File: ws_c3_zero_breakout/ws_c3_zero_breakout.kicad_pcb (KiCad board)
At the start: 2 copper layers, 27 x 30 mm, 10 parts, among them J1 LEFT WING, J2 RIGHT WING, U1 QMI8658C, U2 QMC5883L

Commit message: comment and label change
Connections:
- net /GP20 renamed /UART0_RX
- net /GP21 renamed /UART0_TX
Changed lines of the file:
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@@
 			(layers "*.Cu" "*.Mask")
 			(remove_unused_layers no)
-			(net "/GP20")
+			(net "/UART0_RX")
 			(pinfunction "Pin_8_8")
 			(pintype "passive+no_connect")
@@
 			(layers "*.Cu" "*.Mask")
 			(remove_unused_layers no)
-			(net "/GP21")
+			(net "/UART0_TX")
 			(pinfunction "Pin_9_9")
 			(pintype "passive+no_connect")
@@
 		(effects
 			(font
-				(size 1 1)
+				(size 0.8 0.8)
 				(thickness 0.1)
 			)

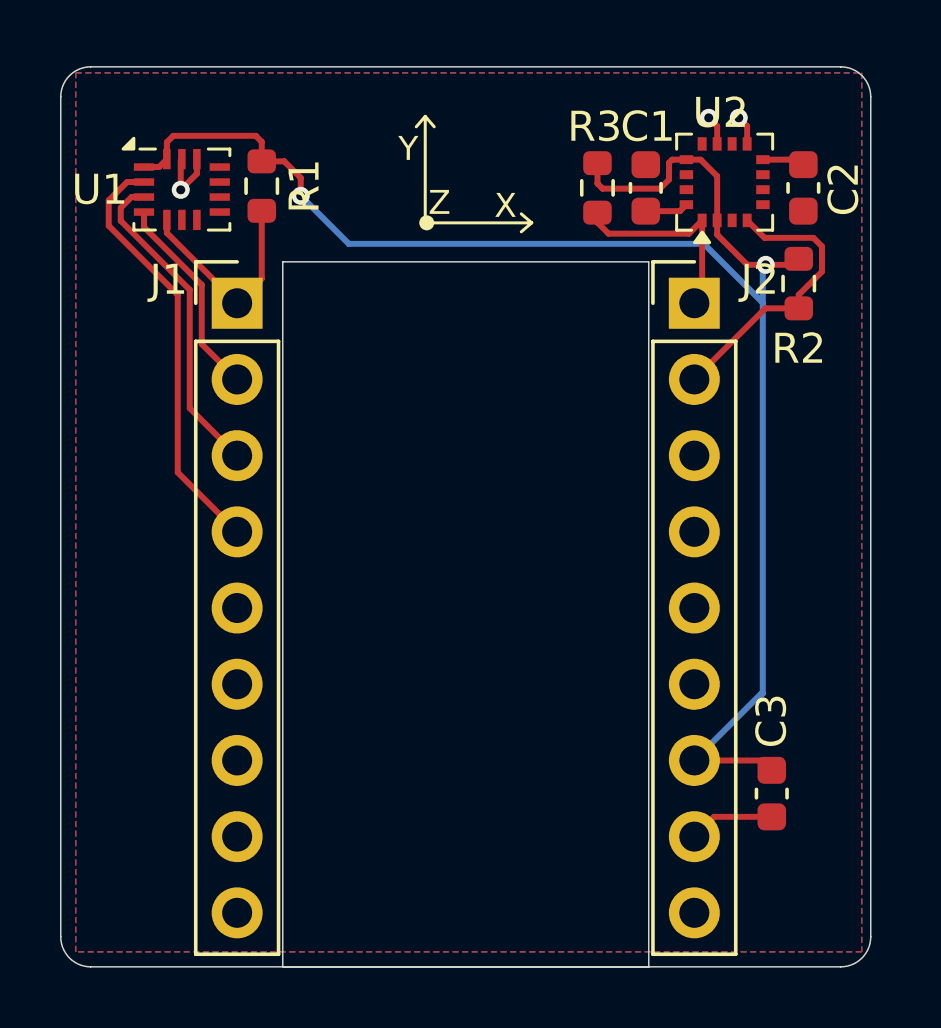
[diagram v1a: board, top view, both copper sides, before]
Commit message: board edgecut fix
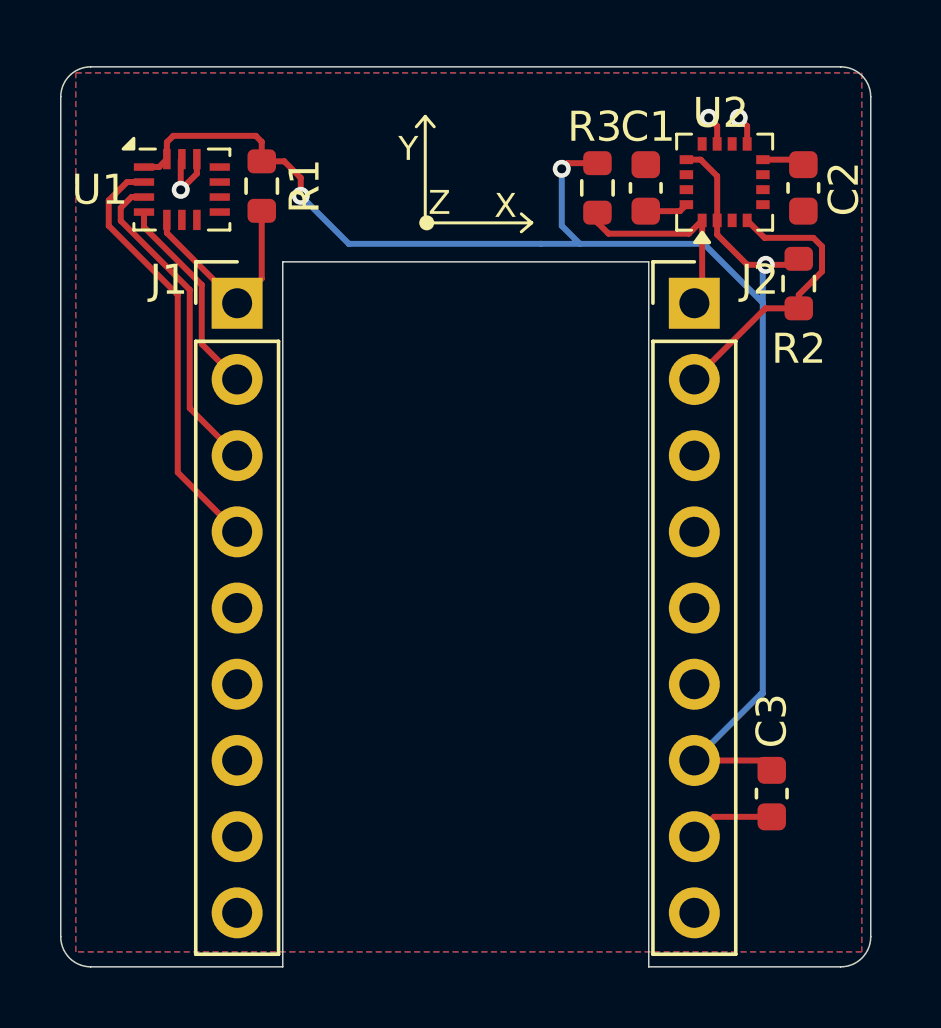
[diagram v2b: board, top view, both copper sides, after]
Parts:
- added REF**: OSHW-Logo2_7.3x6mm_SilkScreen, Symbol:OSHW-Logo2_7.3x6mm_SilkScreen, B.Cu at (100.0, 46.9)
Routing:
- net /3V3: track 55.5 -> 55.1 mm, vias 2 -> 3

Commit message: fixing major pin map  bug in symbol
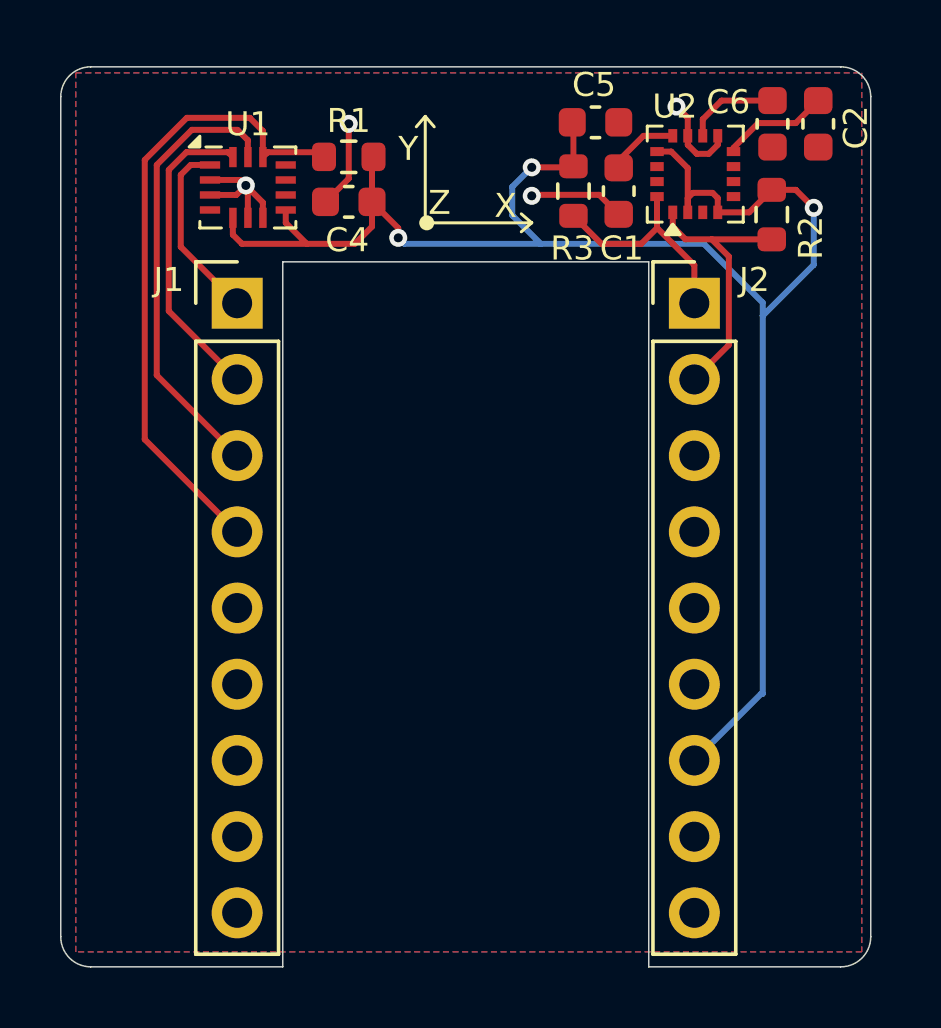
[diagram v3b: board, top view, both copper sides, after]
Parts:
- removed C3: 1uF, Capacitor_SMD:C_0603_1608Metric
- removed REF**: OSHW-Logo2_7.3x6mm_SilkScreen, Symbol:OSHW-Logo2_7.3x6mm_SilkScreen
- added C4: 100nF, Capacitor_SMD:C_0603_1608Metric, F.Cu at (105.1, 48.0)
- added C5: 100nF, Capacitor_SMD:C_0603_1608Metric, F.Cu at (113.3, 45.4)
- added C6: 4.7uF, Capacitor_SMD:C_0603_1608Metric, F.Cu at (119.2, 45.4)
- moved R1 3.06 mm to (105.1, 46.5), turned to 180 degrees
- moved R2 2.47 mm to (119.2, 48.4)
- moved U1 2.20 mm to (101.7, 47.5)
- moved C2 2.19 mm to (120.8, 45.4)
- moved U2 1.02 mm to (116.7, 47.1)
- moved C1 0.91 mm to (114.1, 47.6), turned to 90 degrees
- moved R3 0.81 mm to (112.6, 47.6)
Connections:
- J1 pad 1: /QMI8658C_NCS -> /QMI8658C_MISO
- J1 pad 2: /QMI8658C_MISO -> /QMI8658C_MOSI
- J1 pad 3: /QMI8658C_MOSI -> /QMI8658C_SCLK
- J1 pad 4: /QMI8658C_SCLK -> /QMI8658C_NCS
- J2 pad 1: /QMC5883L_SCL -> /QMC5883L_SDA
- J2 pad 2: /QMC5883L_SDA -> /QMC5883L_SCL
- R2 pad 2: /QMC5883L_SDA -> /QMC5883L_SCL
- R3 pad 2: /QMC5883L_SCL -> /QMC5883L_SDA
- U1 pad 1: /3V3 -> /QMI8658C_MISO
- U1 pad 12: /GND -> /QMI8658C_NCS
- U1 pad 13: /GND -> /QMI8658C_SCLK
- U1 pad 14: /3V3 -> /QMI8658C_MOSI
- U1 pad 2: /QMI8658C_SCLK -> /GND
- U1 pad 3: /QMI8658C_MOSI -> /GND
- U1 pad 4: /QMI8658C_MISO -> unconnected-(U1-INT1-Pad4)
- U1 pad 5: /QMI8658C_NCS -> /3V3
- U1 pad 6: unconnected-(U1-INT2-Pad6) -> /GND
- U1 pad 7: unconnected-(U1-INT1-Pad7) -> /GND
- U1 pad 8: unconnected-(U1-NC-Pad8) -> /3V3
- U2 pad 10: unconnected-(U2-NC-Pad10) -> Net-(U2-C1)
- U2 pad 12: unconnected-(U2-NC-Pad12) -> Net-(U2-SETC)
- U2 pad 16: Net-(U2-SETC) -> /QMC5883L_SDA
- U2 pad 4: /QMC5883L_SDA -> /3V3
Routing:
- net /QMI8658C_NCS: track 7.17 -> 21.4 mm
- net /GND: track 7.11 -> 14.1 mm, vias 3 -> 4
- net /3V3: track 55.1 -> 59.2 mm
- net Net-(U2-C1): track 0.00 -> 3.13 mm
- net /QMC5883L_SCL: track 7.02 -> 9.33 mm
- net Net-(U2-SETP): track 1.42 -> 3.60 mm
- net /QMC5883L_SDA: track 9.70 -> 8.32 mm
- net Net-(U2-SETC): track 1.44 -> 2.38 mm
- net /QMI8658C_SCLK: track 14.2 -> 15.0 mm
- net /QMI8658C_MISO: track 6.87 -> 6.17 mm

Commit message: adding bmp280
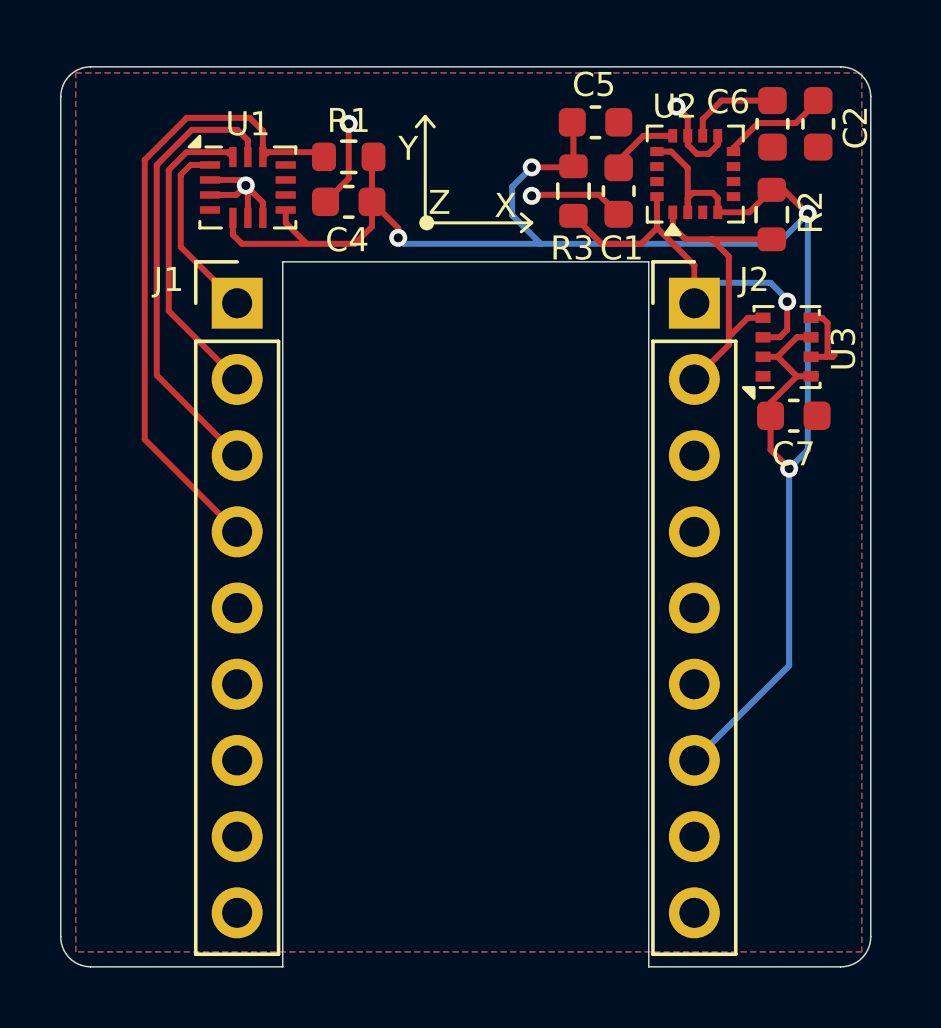
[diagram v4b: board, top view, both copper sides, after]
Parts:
- added C7: 100nF, Capacitor_SMD:C_0603_1608Metric, F.Cu at (119.9, 55.1)
- added U3: BMP280, Package_LGA:Bosch_LGA-8_2x2.5mm_P0.65mm_ClockwisePinNumbering, F.Cu at (119.7, 52.8)
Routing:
- net /3V3: track 59.2 -> 66.6 mm, vias 3 -> 4
- net /QMC5883L_SDA: track 8.32 -> 13.9 mm, vias 0 -> 1
- net /GND: track 14.1 -> 16.7 mm
- net /QMC5883L_SCL: track 9.33 -> 11.2 mm
